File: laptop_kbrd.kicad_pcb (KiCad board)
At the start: 2 copper layers, 141.3 x 42.1 mm, 125 parts, among them CON1 AVR-ISP-6-DR, CON2 AVR-ISP-6-DR, CON3 AVR-ISP-6-DR, K1 CASE_OPEN, K2 CASE_OPEN, Q1 MOSFET_N, Q10 MOSFET_N, Q11 MOSFET_N, Q2 MOSFET_N, Q3 MOSFET_N, Q4 MOSFET_N, Q5 MOSFET_N, Q6 MOSFET_N, Q7 MOSFET_N, Q8 ALS_PT19, Q9 MOSFET_N, SW1 MCU_RST, SW2 BT_ASSCN, SW3 POWER, SW4 CASE_PUSH, SW5 MCU_RST, SW6 MCU_RST, SW7 SPST, U1 ATMEGA32U4-AU, U10 NHD-0440AZ-FL-YBW, U11 NRF24L01+, U12 ATAES132A, U13 AT97SC3205T, U14 TUSB2046BVFR, U15 MAX6749, U16 BME280, U17 TPS2041B, U18 LVDS_HEADER, U2 RT9706, U3 ATMEGA32U4, U4 0WX4JF, U5 XF2M-3015-1A, U6 ATMEGA32U4, U7 USB_CAM, U8 EPAPER_V2, U9 USB_A_FEMALE, X1 XTAL 16MHz, X2 XTAL 16MHz, X3 XTAL 16MHz, X4 6MHz

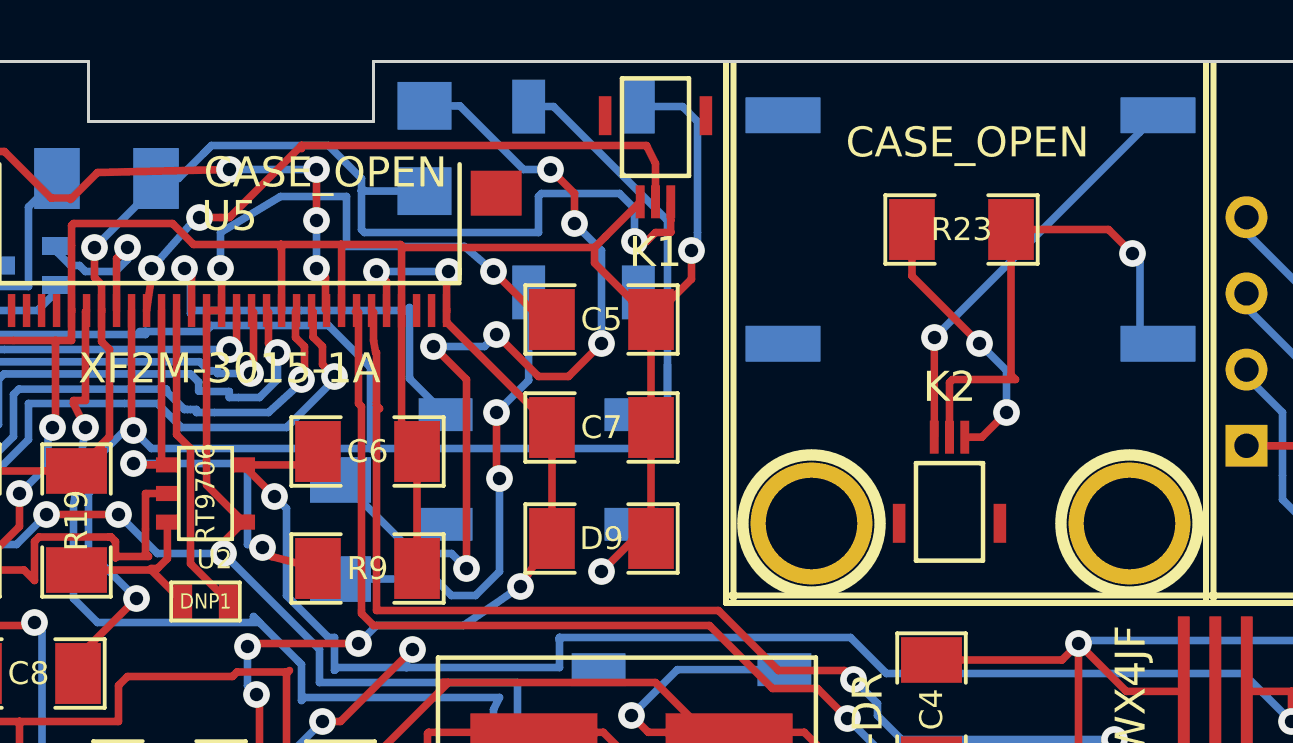
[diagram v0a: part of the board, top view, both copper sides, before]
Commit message: Modified footprint for 3pin_FPC connector (K1 and K2).
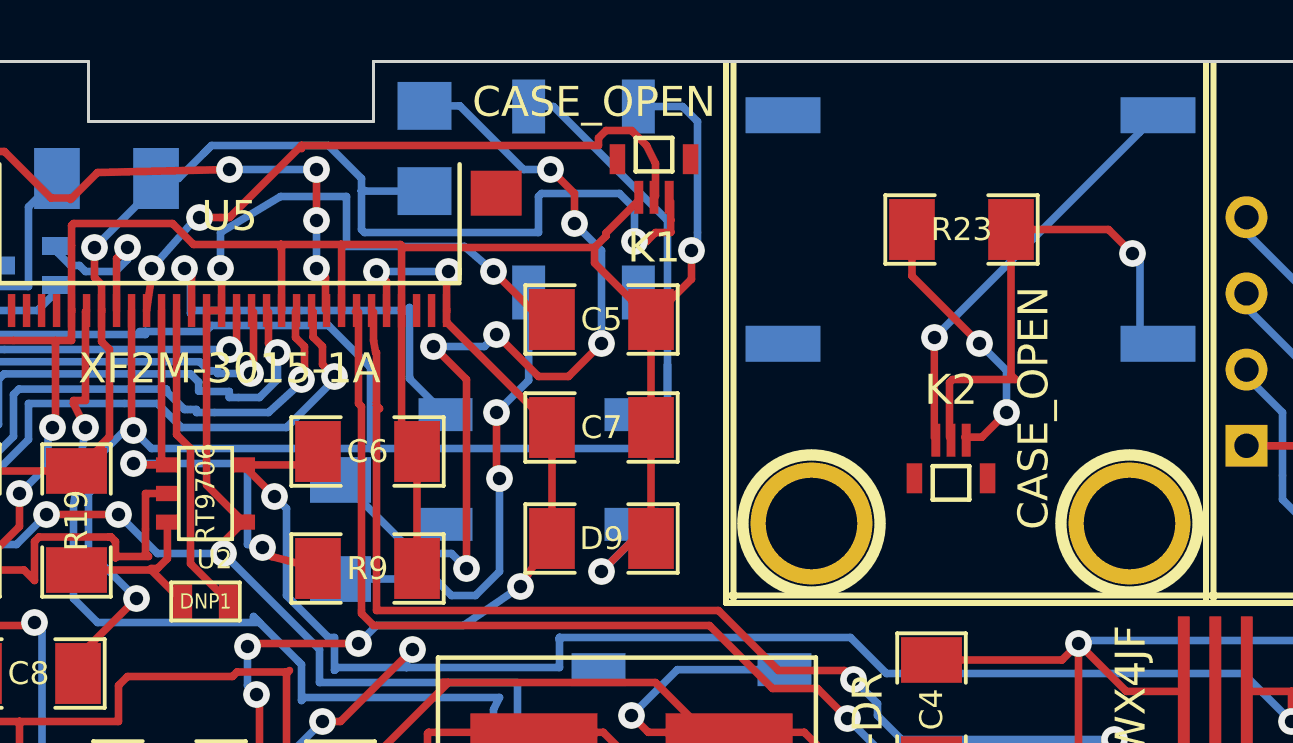
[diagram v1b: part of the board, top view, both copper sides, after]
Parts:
- moved K1 0.16 mm to (163.1, 122.3)
- moved K2 0.11 mm to (173.0, 133.8)
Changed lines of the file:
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@@
     (thickness 1.6)
     (drawings 43)
-    (tracks 3328)
+    (tracks 3336)
     (zones 0)
     (modules 125)
@@
     (mod_text_size 1 1)
     (mod_text_width 0.15)
-    (pad_size 2.99974 2.99974)
-    (pad_drill 2)
+    (pad_size 0.52 1)
+    (pad_drill 0)
     (pad_to_mask_clearance 0)
     (aux_axis_origin 0 0)
     (visible_elements 7FFFFFFF)
     (pcbplotparams
-      (layerselection 536838145)
-      (usegerberextensions true)
-      (excludeedgelayer true)
+      (layerselection 268468224)
+      (usegerberextensions false)
+      (excludeedgelayer false)
       (linewidth 0.150000)
       (plotframeref false)
@@
       (padsonsilk true)
       (subtractmaskfromsilk false)
-      (outputformat 1)
+      (outputformat 2)
       (mirror false)
       (drillshape 0)
       (scaleselection 1)
-      (outputdirectory gerbers01/))
+      (outputdirectory ./))
   )
   (net 0 "")
@@
     )
   )
-  (module 3pin_FPC (layer F.Cu)
-    (at 163.15 122.45 180)
-    (fp_text reference K1 (at 0 -3.3528 180) (layer F.SilkS)
-      (effects (font (size 1 1) (thickness 0.15)))
-    )
-    (fp_text value CASE_OPEN (at 11 -0.7 180) (layer F.SilkS)
-      (effects (font (size 1 1) (thickness 0.15)))
-    )
-    (fp_line (start -1.1176 -0.8128) (end 1.016 -0.8128) (layer F.SilkS) (width 0.15))
-    (fp_line (start 1.016 -0.8128) (end 1.1176 -0.8128) (layer F.SilkS) (width 0.15))
-    (fp_line (start 1.1176 -0.8128) (end 1.1176 2.4384) (layer F.SilkS) (width 0.15))
-    (fp_line (start 1.1176 2.4384) (end -1.1176 2.4384) (layer F.SilkS) (width 0.15))
-    (fp_line (start -1.1176 2.4384) (end -1.1176 -0.8128) (layer F.SilkS) (width 0.15))
-    (pad 1 smd rect (at -0.508 -1.6764 180) (size 0.3 1.1)
-      (layers F.Cu F.Paste F.Mask)
-      (net 1 /3.3V_DELAYED)
-      (clearance 0.1)
-    )
-    (pad 2 smd rect (at 0 -1.6764 180) (size 0.3 1.1)
-      (layers F.Cu F.Paste F.Mask)
-      (net 22 /KEY_COL3)
-      (clearance 0.1)
-    )
-    (pad 3 smd rect (at 0.508 -1.6764 180) (size 0.3 1.1)
-      (layers F.Cu F.Paste F.Mask)
-      (net 92 GND)
-      (clearance 0.1)
-    )
-    (pad 4 smd rect (at -1.68 1.1936 180) (size 0.42 1.3)
-      (layers F.Cu F.Paste F.Mask)
-    )
-    (pad 4 smd rect (at 1.68 1.1936 180) (size 0.42 1.3)
-      (layers F.Cu F.Paste F.Mask)
-    )
-  )
   (module SOT23-5_DR (layer F.Cu)
     (at 148.15 133.85 270)
@@
     )
   )
-  (module 3pin_FPC (layer F.Cu)
-    (at 172.95 133.65)
-    (fp_text reference K2 (at 0 -3.3528) (layer F.SilkS)
-      (effects (font (size 1 1) (thickness 0.15)))
-    )
-    (fp_text value CASE_OPEN (at 0.6 -11.5) (layer F.SilkS)
-      (effects (font (size 1 1) (thickness 0.15)))
-    )
-    (fp_line (start -1.1176 -0.8128) (end 1.016 -0.8128) (layer F.SilkS) (width 0.15))
-    (fp_line (start 1.016 -0.8128) (end 1.1176 -0.8128) (layer F.SilkS) (width 0.15))
-    (fp_line (start 1.1176 -0.8128) (end 1.1176 2.4384) (layer F.SilkS) (width 0.15))
-    (fp_line (start 1.1176 2.4384) (end -1.1176 2.4384) (layer F.SilkS) (width 0.15))
-    (fp_line (start -1.1176 2.4384) (end -1.1176 -0.8128) (layer F.SilkS) (width 0.15))
-    (pad 1 smd rect (at -0.508 -1.6764) (size 0.3 1.1)
-      (layers F.Cu F.Paste F.Mask)
-      (net 144 N-0000055)
-      (clearance 0.1)
-    )
-    (pad 2 smd rect (at 0 -1.6764) (size 0.3 1.1)
-      (layers F.Cu F.Paste F.Mask)
-      (net 145 N-0000056)
-      (clearance 0.1)
-    )
-    (pad 3 smd rect (at 0.508 -1.6764) (size 0.3 1.1)
-      (layers F.Cu F.Paste F.Mask)
-      (net 146 N-0000057)
-      (clearance 0.1)
-    )
-    (pad 4 smd rect (at -1.68 1.1936) (size 0.42 1.3)
-      (layers F.Cu F.Paste F.Mask)
-    )
-    (pad 4 smd rect (at 1.68 1.1936) (size 0.42 1.3)
-      (layers F.Cu F.Paste F.Mask)
-    )
-  )
   (module PUSH_BT (layer B.Cu)
     (at 173.65 125.05)
@@
     )
   )
+  (module 3pin_FPC (layer F.Cu)
+    (at 163.1 122.3 180)
+    (fp_text reference K1 (at 0 -3.3528 180) (layer F.SilkS)
+      (effects (font (size 1 1) (thickness 0.15)))
+    )
+    (fp_text value CASE_OPEN (at 2 1.5 180) (layer F.SilkS)
+      (effects (font (size 1 1) (thickness 0.15)))
+    )
+    (fp_line (start -0.6096 -0.8128) (end -0.6096 0.3048) (layer F.SilkS) (width 0.15))
+    (fp_line (start -0.6096 0.3048) (end 0.6096 0.3048) (layer F.SilkS) (width 0.15))
+    (fp_line (start 0.6096 0.3048) (end 0.6096 -0.8128) (layer F.SilkS) (width 0.15))
+    (fp_line (start 0.6096 -0.8128) (end -0.6096 -0.8128) (layer F.SilkS) (width 0.15))
+    (pad 1 smd rect (at -0.508 -1.6764 180) (size 0.3 1.1)
+      (layers F.Cu F.Paste F.Mask)
+      (net 1 /3.3V_DELAYED)
+      (clearance 0.1)
+    )
+    (pad 2 smd rect (at 0 -1.6764 180) (size 0.3 1.1)
+      (layers F.Cu F.Paste F.Mask)
+      (net 22 /KEY_COL3)
+      (clearance 0.1)
+    )
+    (pad 3 smd rect (at 0.508 -1.6764 180) (size 0.3 1.1)
+      (layers F.Cu F.Paste F.Mask)
+      (net 92 GND)
+      (clearance 0.1)
+    )
+    (pad 4 smd rect (at -1.2192 -0.4064 180) (size 0.52 1)
+      (layers F.Cu F.Paste F.Mask)
+    )
+    (pad 4 smd rect (at 1.2192 -0.4064 180) (size 0.52 1)
+      (layers F.Cu F.Paste F.Mask)
+    )
+  )
+  (module 3pin_FPC (layer F.Cu)
+    (at 173 133.75)
+    (fp_text reference K2 (at 0 -3.3528) (layer F.SilkS)
+      (effects (font (size 1 1) (thickness 0.15)))
+    )
+    (fp_text value CASE_OPEN (at 2.75 -2.75 90) (layer F.SilkS)
+      (effects (font (size 1 1) (thickness 0.15)))
+    )
+    (fp_line (start -0.6096 -0.8128) (end -0.6096 0.3048) (layer F.SilkS) (width 0.15))
+    (fp_line (start -0.6096 0.3048) (end 0.6096 0.3048) (layer F.SilkS) (width 0.15))
+    (fp_line (start 0.6096 0.3048) (end 0.6096 -0.8128) (layer F.SilkS) (width 0.15))
+    (fp_line (start 0.6096 -0.8128) (end -0.6096 -0.8128) (layer F.SilkS) (width 0.15))
+    (pad 1 smd rect (at -0.508 -1.6764) (size 0.3 1.1)
+      (layers F.Cu F.Paste F.Mask)
+      (net 144 N-0000055)
+      (clearance 0.1)
+    )
+    (pad 2 smd rect (at 0 -1.6764) (size 0.3 1.1)
+      (layers F.Cu F.Paste F.Mask)
+      (net 145 N-0000056)
+      (clearance 0.1)
+    )
+    (pad 3 smd rect (at 0.508 -1.6764) (size 0.3 1.1)
+      (layers F.Cu F.Paste F.Mask)
+      (net 146 N-0000057)
+      (clearance 0.1)
+    )
+    (pad 4 smd rect (at -1.2192 -0.4064) (size 0.52 1)
+      (layers F.Cu F.Paste F.Mask)
+    )
+    (pad 4 smd rect (at 1.2192 -0.4064) (size 0.52 1)
+      (layers F.Cu F.Paste F.Mask)
+    )
+  )
   (gr_line (start 165.75 119.5) (end 165.75 137.5) (angle 90) (layer B.SilkS) (width 0.2))
   (gr_line (start 165.5 137.5) (end 165.5 119.5) (angle 90) (layer B.SilkS) (width 0.2))
@@
   (segment (start 146.6856 127.7516) (end 146.6856 132.7031) (width 0.254) (layer F.Cu) (net 21))
   (segment (start 146.6856 132.7031) (end 146.88 132.8975) (width 0.254) (layer F.Cu) (net 21))
+  (segment (start 163.15 122.85) (end 163.15 123.9264) (width 0.254) (layer F.Cu) (net 22))
+  (segment (start 161.25 122.25) (end 161.25 122) (width 0.254) (layer F.Cu) (net 22))
+  (segment (start 162.35 121.75) (end 162.85 122.25) (width 0.254) (layer F.Cu) (net 22))
+  (segment (start 161.5 121.75) (end 162.35 121.75) (width 0.254) (layer F.Cu) (net 22))
+  (segment (start 161.25 122) (end 161.5 121.75) (width 0.254) (layer F.Cu) (net 22))
+  (segment (start 162.85 122.25) (end 163.15 122.85) (width 0.254) (layer F.Cu) (net 22))
+  (segment (start 151.35 122.25) (end 161.25 122.25) (width 0.254) (layer F.Cu) (net 22))
+  (segment (start 163.15 123.9264) (end 163.1 123.9764) (width 0.254) (layer F.Cu) (net 22))
   (segment (start 147.95 124.65) (end 148.65 124.65) (width 0.254) (layer F.Cu) (net 22))
   (segment (start 148.95 124.65) (end 151.35 122.25) (width 0.254) (layer F.Cu) (net 22))
@@
   (segment (start 151.35 122.35) (end 151.35 122.25) (width 0.254) (layer F.Cu) (net 22))
   (segment (start 146.1856 127.7516) (end 146.3856 126.3856) (width 0.254) (layer F.Cu) (net 22))
-  (segment (start 163.15 122.85) (end 163.15 124.1264) (width 0.254) (layer F.Cu) (net 22))
-  (segment (start 162.85 122.25) (end 163.15 122.85) (width 0.254) (layer F.Cu) (net 22))
-  (segment (start 151.35 122.25) (end 162.85 122.25) (width 0.254) (layer F.Cu) (net 22))
   (via (at 147.95 124.65) (size 0.889) (layers F.Cu B.Cu) (net 22))
   (segment (start 147.85 124.65) (end 147.95 124.65) (width 0.254) (layer B.Cu) (net 22))
@@
   (segment (start 211.242998 161.057002) (end 172.857002 161.057002) (width 0.254) (layer B.Cu) (net 91))
   (segment (start 213.05 159.25) (end 211.242998 161.057002) (width 0.254) (layer B.Cu) (net 91))
+  (segment (start 162.592 123.9764) (end 162.592 124.0764) (width 0.254) (layer F.Cu) (net 92))
+  (segment (start 161.5 125.1684) (end 161.5 125.2684) (width 0.254) (layer F.Cu) (net 92))
+  (segment (start 162.592 124.0764) (end 161.5 125.1684) (width 0.254) (layer F.Cu) (net 92))
   (segment (start 162.15 157.35) (end 162.15 159.101) (width 0.254) (layer F.Cu) (net 92))
   (segment (start 162.15 159.101) (end 162.399 159.35) (width 0.254) (layer F.Cu) (net 92))
@@
   (segment (start 163.8212 143.3788) (end 162.55 144.65) (width 0.254) (layer B.Cu) (net 92))
   (segment (start 154.6856 125.65) (end 161.1184 125.65) (width 0.254) (layer F.Cu) (net 92))
-  (segment (start 161.1184 125.65) (end 161.4842 125.2842) (width 0.254) (layer F.Cu) (net 92))
-  (segment (start 161.4842 125.2842) (end 162.642 124.1264) (width 0.254) (layer F.Cu) (net 92))
+  (segment (start 161.1184 125.65) (end 161.5 125.2684) (width 0.254) (layer F.Cu) (net 92))
+  (segment (start 161.5 125.2684) (end 161.4842 125.2842) (width 0.254) (layer F.Cu) (net 92))
   (segment (start 154.6856 125.5856) (end 154.6856 125.65) (width 0.254) (layer F.Cu) (net 92))
   (segment (start 154.65 125.55) (end 154.6856 125.5856) (width 0.254) (layer F.Cu) (net 92))

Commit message: Added decals
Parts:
- added G***: LOGO, LOGO, B.Cu at (167.2, 153.8)
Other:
- board text added: "NOVENA-X"
- board text added: "PROJECT"
- board text added: "http://rightshift.info"
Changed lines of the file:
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@@
     (area 134.999999 118.755334 276.400001 162.232)
     (thickness 1.6)
-    (drawings 43)
+    (drawings 46)
     (tracks 3336)
     (zones 0)
-    (modules 125)
+    (modules 126)
     (nets 166)
   )
@@
     (visible_elements 7FFFFFFF)
     (pcbplotparams
-      (layerselection 268468224)
-      (usegerberextensions false)
-      (excludeedgelayer false)
+      (layerselection 536838145)
+      (usegerberextensions true)
+      (excludeedgelayer true)
       (linewidth 0.150000)
       (plotframeref false)
@@
       (padsonsilk true)
       (subtractmaskfromsilk false)
-      (outputformat 2)
+      (outputformat 1)
       (mirror false)
       (drillshape 0)
       (scaleselection 1)
-      (outputdirectory ./))
+      (outputdirectory gerbers01/))
   )
   (net 0 "")
@@
     )
   )
+  (module LOGO (layer B.Cu)
+    (at 167.2 153.8)
+    (fp_text reference G*** (at 0 -9.22782) (layer B.SilkS) hide
+      (effects (font (size 1.524 1.524) (thickness 0.3048)) (justify mirror))
+    )
+    (fp_text value LOGO (at 12.9 4.4) (layer B.SilkS) hide
+      (effects (font (size 1.524 1.524) (thickness 0.3048)) (justify mirror))
+    )
+    (fp_poly (pts (xy 7.2009 -0.4064) (xy 7.17804 0.57912) (xy 7.15518 1.56718) (xy 6.24586 1.72974)
+      (xy 5.33908 1.8923) (xy 5.03936 2.64414) (xy 4.7371 3.39598) (xy 5.26034 4.16052)
+      (xy 5.78358 4.92252) (xy 5.07238 5.63118) (xy 4.36118 6.3373) (xy 3.61188 5.82168)
+      (xy 2.86512 5.30606) (xy 2.47142 5.49656) (xy 2.2479 5.59308) (xy 2.09296 5.62864)
+      (xy 2.05232 5.61594) (xy 2.01422 5.51942) (xy 1.92024 5.29082) (xy 1.78308 4.95808)
+      (xy 1.61036 4.54152) (xy 1.41478 4.07162) (xy 1.39446 4.02082) (xy 0.75946 2.49682)
+      (xy 0.99314 2.32918) (xy 1.45796 1.92024) (xy 1.76784 1.48336) (xy 1.93294 0.99568)
+      (xy 1.97104 0.5842) (xy 1.89738 0.01778) (xy 1.6764 -0.48006) (xy 1.3208 -0.89154)
+      (xy 0.84836 -1.19888) (xy 0.51308 -1.32588) (xy -0.02032 -1.40208) (xy -0.5334 -1.32588)
+      (xy -1.00076 -1.1176) (xy -1.39954 -0.79502) (xy -1.70688 -0.37592) (xy -1.89484 0.12192)
+      (xy -1.94818 0.58166) (xy -1.87706 1.11506) (xy -1.66116 1.59512) (xy -1.28524 2.04216)
+      (xy -1.17094 2.14884) (xy -0.74676 2.51968) (xy -1.39954 4.09448) (xy -1.6002 4.57454)
+      (xy -1.78054 4.99364) (xy -1.9304 5.33146) (xy -2.04216 5.56514) (xy -2.10058 5.66928)
+      (xy -2.10566 5.67182) (xy -2.20726 5.63118) (xy -2.3876 5.53212) (xy -2.43586 5.50164)
+      (xy -2.63906 5.39242) (xy -2.78638 5.33654) (xy -2.80416 5.334) (xy -2.9083 5.37972)
+      (xy -3.11658 5.50164) (xy -3.39344 5.67944) (xy -3.57124 5.79882) (xy -3.87096 5.99948)
+      (xy -4.1275 6.15696) (xy -4.30022 6.2484) (xy -4.34848 6.26618) (xy -4.445 6.20776)
+      (xy -4.63296 6.05282) (xy -4.87934 5.82676) (xy -5.1054 5.60324) (xy -5.76326 4.94284)
+      (xy -5.25272 4.18846) (xy -5.04444 3.87096) (xy -4.8768 3.60172) (xy -4.77012 3.41376)
+      (xy -4.74472 3.34518) (xy -4.7752 3.23342) (xy -4.85648 3.00482) (xy -4.97332 2.7051)
+      (xy -5.02158 2.58318) (xy -5.29844 1.90754) (xy -6.22808 1.73736) (xy -7.15518 1.56464)
+      (xy -7.17804 0.64262) (xy -7.18058 0.254) (xy -7.17042 -0.06858) (xy -7.14756 -0.28702)
+      (xy -7.12216 -0.36322) (xy -7.0104 -0.41148) (xy -6.7691 -0.4826) (xy -6.43636 -0.56134)
+      (xy -6.13918 -0.62484) (xy -5.23494 -0.80518) (xy -4.94284 -1.48844) (xy -4.6482 -2.1717)
+      (xy -5.19938 -2.97942) (xy -5.75056 -3.78714) (xy -5.07238 -4.47548) (xy -4.79806 -4.7498)
+      (xy -4.56692 -4.97078) (xy -4.40182 -5.1181) (xy -4.33578 -5.16382) (xy -4.24688 -5.12064)
+      (xy -4.04876 -4.99618) (xy -3.7719 -4.81584) (xy -3.48742 -4.62026) (xy -2.69748 -4.0767)
+      (xy -2.09042 -4.33324) (xy -1.79324 -4.46278) (xy -1.55448 -4.57454) (xy -1.4224 -4.64566)
+      (xy -1.41224 -4.65328) (xy -1.36906 -4.75996) (xy -1.30302 -4.99364) (xy -1.22682 -5.3213)
+      (xy -1.15824 -5.64134) (xy -0.97282 -6.56082) (xy 0.01524 -6.58622) (xy 1.00584 -6.60908)
+      (xy 1.06172 -6.28904) (xy 1.10744 -6.04774) (xy 1.17348 -5.70992) (xy 1.24968 -5.34416)
+      (xy 1.2573 -5.30352) (xy 1.397 -4.63804) (xy 2.07264 -4.35864) (xy 2.74828 -4.07924)
+      (xy 3.52552 -4.6228) (xy 3.84556 -4.8387) (xy 4.1148 -5.0165) (xy 4.30276 -5.1308)
+      (xy 4.37642 -5.16382) (xy 4.46278 -5.10794) (xy 4.63804 -4.95554) (xy 4.87934 -4.72948)
+      (xy 5.1181 -4.49072) (xy 5.78866 -3.81762) (xy 5.23748 -2.98958) (xy 4.6863 -2.159)
+      (xy 4.94538 -1.56718) (xy 5.08 -1.27) (xy 5.19176 -1.0287) (xy 5.26288 -0.889)
+      (xy 5.26796 -0.88138) (xy 5.37718 -0.81534) (xy 5.60324 -0.74422) (xy 5.85978 -0.68326)
+      (xy 6.22554 -0.61214) (xy 6.59384 -0.53594) (xy 6.79704 -0.49276) (xy 7.2009 -0.4064)
+      (xy 7.2009 -0.4064)) (layer B.SilkS) (width 0.00254))
+  )
+  (gr_text NOVENA-X (at 205.3 148.2) (layer B.SilkS)
+    (effects (font (size 6 6) (thickness 1.2)) (justify mirror))
+  )
+  (gr_text http://rightshift.info (at 204.4 155) (layer B.SilkS)
+    (effects (font (size 3 3) (thickness 0.6)) (justify mirror))
+  )
+  (gr_text PROJECT (at 228.5 141.6) (layer B.SilkS)
+    (effects (font (size 3 3) (thickness 0.6)) (justify left mirror))
+  )
   (gr_line (start 165.75 119.5) (end 165.75 137.5) (angle 90) (layer B.SilkS) (width 0.2))
